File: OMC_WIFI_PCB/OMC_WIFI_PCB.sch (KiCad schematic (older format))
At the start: 19 parts, among them J1 ESP32_Left, J10 Control_ACS712, J11 Control_ZMPT101B, J2 ESP32_Right, J3 Power_In, J4 Switch, J5 Pins_FT232R, J6 Line_Relay, J7 Control_Relay, J8 Line_ACS712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

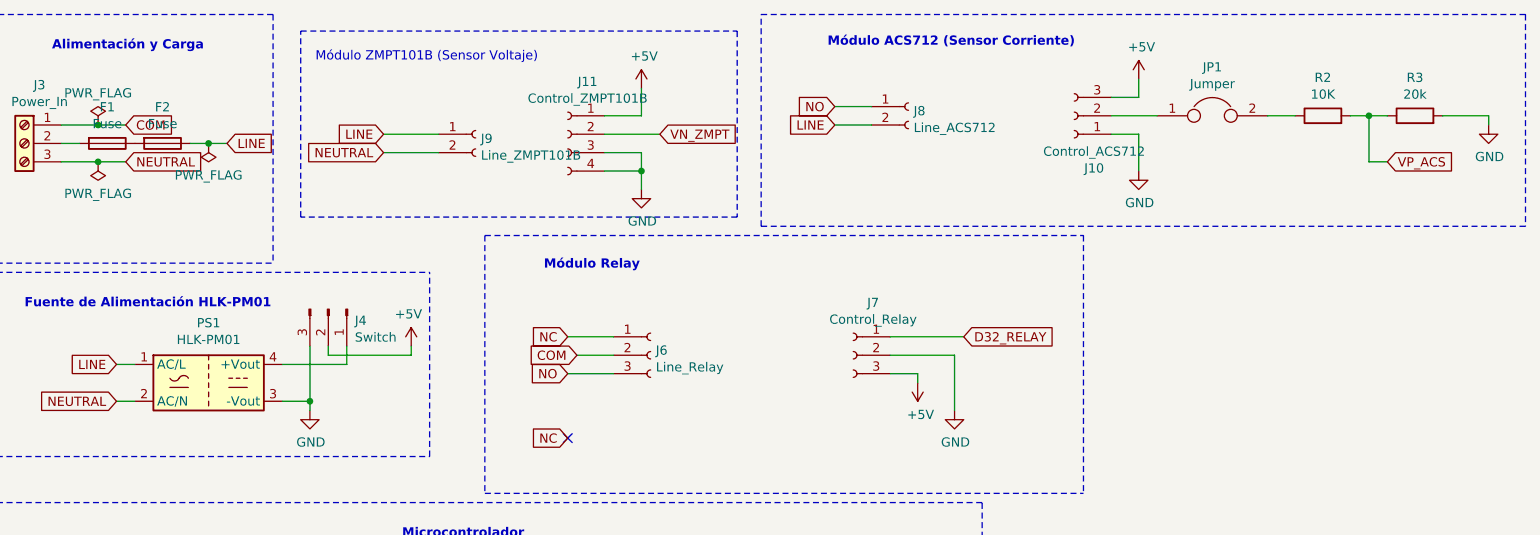
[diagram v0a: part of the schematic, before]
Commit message: Diseño PCB
+ Archivos Gerber y Drill
- Divisor de tensión del ACS712
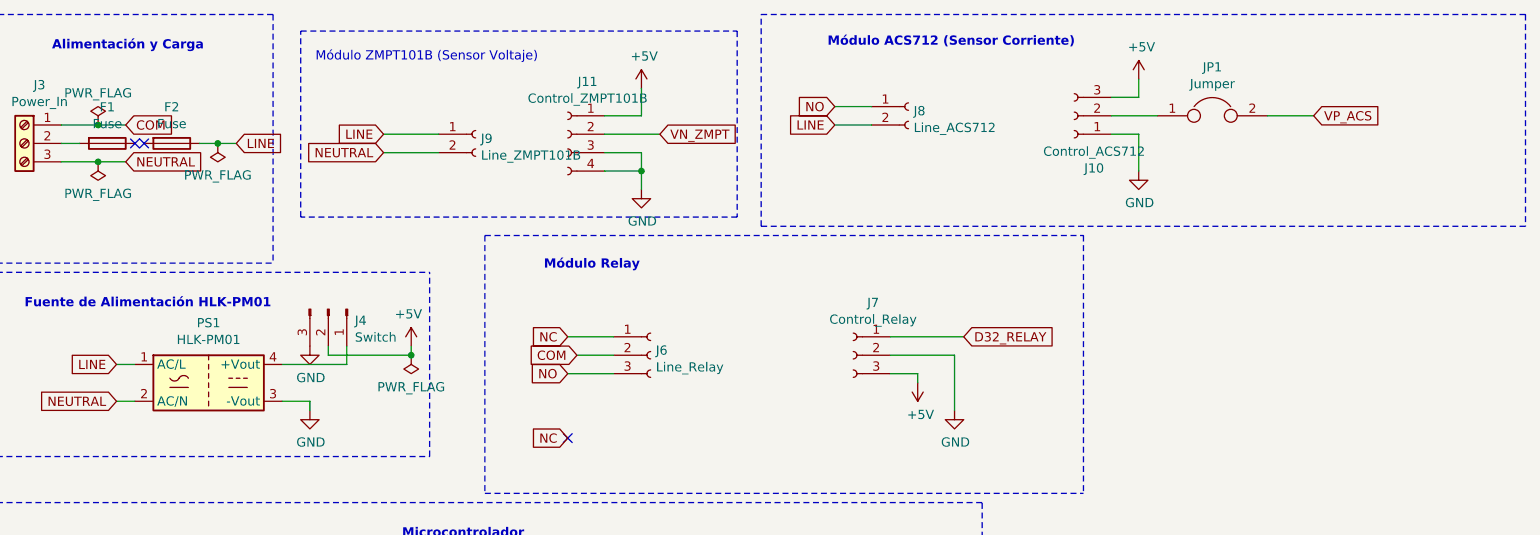
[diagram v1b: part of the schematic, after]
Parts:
- removed R2: 10K, Resistor_SMD:R_2010_5025Metric_Pad1.40x2.65mm_HandSolder, symbol Device:R
- removed R3: 20k, Resistor_SMD:R_2010_5025Metric_Pad1.40x2.65mm_HandSolder, symbol Device:R
- JP1: footprint Connector_PinHeader_1.00mm:PinHeader_1x02_P1.00mm_Vertical -> Connector_PinHeader_2.54mm:PinHeader_1x02_P2.54mm_Vertical
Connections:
- net VP_ACS: now also JP1.2
- net at F1.1: no longer F2.2
- no-connect marks 25 -> 27
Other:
- moved on the sheet: F2
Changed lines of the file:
@@
 	1    0    0    -1
 $EndComp
-Text GLabel 8250 1400 2    50   Input ~ 0
-VP_ACS
 $Comp
 L Connector:Conn_01x03_Female J10
@@
 	700  3000 3050 3000
 Wire Wire Line
-	2400 2400 2400 2700
-Connection ~ 2400 2700
-Wire Wire Line
 	2600 2400 2600 2500
 Wire Wire Line
@@
 L power:PWR_FLAG #FLG0103
 U 1 1 62127B9A
-P 1850 1300
-F 0 "#FLG0103" H 1850 1375 50  0001 C CNN
-F 1 "PWR_FLAG" H 1850 1473 50  0000 C CNN
-F 2 "" H 1850 1300 50  0001 C CNN
-F 3 "~" H 1850 1300 50  0001 C CNN
-	1    1850 1300
+P 1900 1300
+F 0 "#FLG0103" H 1900 1375 50  0001 C CNN
+F 1 "PWR_FLAG" H 1900 1473 50  0000 C CNN
+F 2 "" H 1900 1300 50  0001 C CNN
+F 3 "~" H 1900 1300 50  0001 C CNN
+	1    1900 1300
 	1    0    0    1
 $EndComp
 Wire Wire Line
-	1950 1300 1850 1300
-Wire Wire Line
-	1750 1300 1850 1300
-Connection ~ 1850 1300
+	2000 1300 1900 1300
+Wire Wire Line
+	1800 1300 1900 1300
+Connection ~ 1900 1300
 $Comp
 L Device:Fuse F1
@@
 L Device:Fuse F2
 U 1 1 6214DC3E
-P 1600 1300
-F 0 "F2" V 1403 1300 50  0000 C CNN
-F 1 "Fuse" V 1494 1300 50  0000 C CNN
-F 2 "Fuse:Fuse_Littelfuse_395Series" V 1530 1300 50  0001 C CNN
-F 3 "~" H 1600 1300 50  0001 C CNN
-	1    1600 1300
+P 1650 1300
+F 0 "F2" V 1453 1300 50  0000 C CNN
+F 1 "Fuse" V 1544 1300 50  0000 C CNN
+F 2 "Fuse:Fuse_Littelfuse_395Series" V 1580 1300 50  0001 C CNN
+F 3 "~" H 1650 1300 50  0001 C CNN
+	1    1650 1300
 	0    1    1    0
 $EndComp
-Text GLabel 1950 1300 2    50   Input ~ 0
+Text GLabel 2000 1300 2    50   Input ~ 0
 LINE
 Wire Wire Line
@@
 F 0 "JP1" H 7300 1414 50  0000 C CNN
 F 1 "Jumper" H 7300 1323 50  0000 C CNN
-F 2 "Connector_PinHeader_1.00mm:PinHeader_1x02_P1.00mm_Vertical" H 7300 1150 50  0001 C CNN
+F 2 "Connector_PinHeader_2.54mm:PinHeader_1x02_P2.54mm_Vertical" H 7300 1150 50  0001 C CNN
 F 3 "~" H 7300 1150 50  0001 C CNN
 	1    7300 1150
@@
 Wire Wire Line
 	6750 1150 7000 1150
-$Comp
-L Device:R R2
-U 1 1 621CBE6C
-P 7900 1150
-F 0 "R2" V 8107 1150 50  0000 C CNN
-F 1 "10K" V 8016 1150 50  0000 C CNN
-F 2 "Resistor_SMD:R_2010_5025Metric_Pad1.40x2.65mm_HandSolder" V 7830 1150 50  0001 C CNN
-F 3 "~" H 7900 1150 50  0001 C CNN
-	1    7900 1150
-	0    -1   -1   0
-$EndComp
-$Comp
-L Device:R R3
-U 1 1 621CF98B
-P 8400 1150
-F 0 "R3" V 8607 1150 50  0000 C CNN
-F 1 "20k" V 8516 1150 50  0000 C CNN
-F 2 "Resistor_SMD:R_2010_5025Metric_Pad1.40x2.65mm_HandSolder" V 8330 1150 50  0001 C CNN
-F 3 "~" H 8400 1150 50  0001 C CNN
-	1    8400 1150
-	0    -1   -1   0
-$EndComp
+Wire Notes Line
+	4850 600  9000 600
+Wire Notes Line
+	4850 1750 9000 1750
+Wire Notes Line
+	9000 600  9000 1750
+Text GLabel 7850 1150 2    50   Input ~ 0
+VP_ACS
+Wire Wire Line
+	7600 1150 7850 1150
+$Comp
+L power:PWR_FLAG #FLG0104
+U 1 1 62219A74
+P 2950 2450
+F 0 "#FLG0104" H 2950 2525 50  0001 C CNN
+F 1 "PWR_FLAG" H 2950 2623 50  0000 C CNN
+F 2 "" H 2950 2450 50  0001 C CNN
+F 3 "~" H 2950 2450 50  0001 C CNN
+	1    2950 2450
+	1    0    0    1
+$EndComp
+Connection ~ 2950 2450
 $Comp
 L power:GND #PWR0111
-U 1 1 621D76EE
-P 8800 1200
-F 0 "#PWR0111" H 8800 950 50  0001 C CNN
-F 1 "GND" H 8805 1027 50  0000 C CNN
-F 2 "" H 8800 1200 50  0001 C CNN
-F 3 "" H 8800 1200 50  0001 C CNN
-	1    8800 1200
-	1    0    0    -1
-$EndComp
-Wire Wire Line
-	7600 1150 7750 1150
-Wire Wire Line
-	8050 1150 8150 1150
-Wire Wire Line
-	8550 1150 8800 1150
-Wire Wire Line
-	8800 1150 8800 1200
-Wire Wire Line
-	8250 1400 8150 1400
-Wire Wire Line
-	8150 1400 8150 1150
-Connection ~ 8150 1150
-Wire Wire Line
-	8150 1150 8250 1150
-Wire Notes Line
-	4850 600  9000 600
-Wire Notes Line
-	4850 1750 9000 1750
-Wire Notes Line
-	9000 600  9000 1750
+U 1 1 62227D4B
+P 2400 2400
+F 0 "#PWR0111" H 2400 2150 50  0001 C CNN
+F 1 "GND" H 2405 2227 50  0000 C CNN
+F 2 "" H 2400 2400 50  0001 C CNN
+F 3 "" H 2400 2400 50  0001 C CNN
+	1    2400 2400
+	1    0    0    -1
+$EndComp
+NoConn ~ 1450 1300
+NoConn ~ 1500 1300
 $EndSCHEMATC

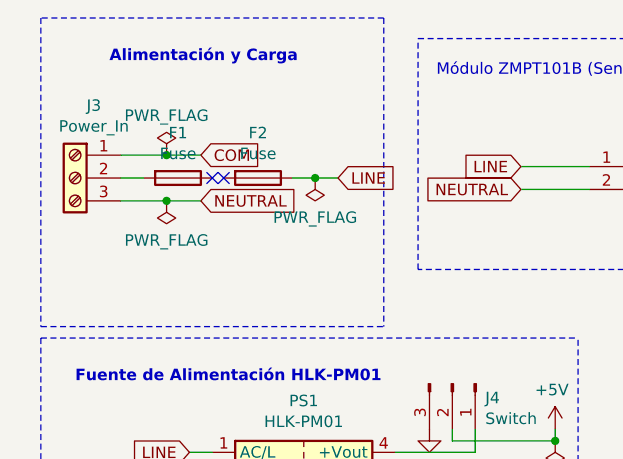
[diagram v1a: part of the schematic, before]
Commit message: Actualización PCB
> Actualización esquemático.
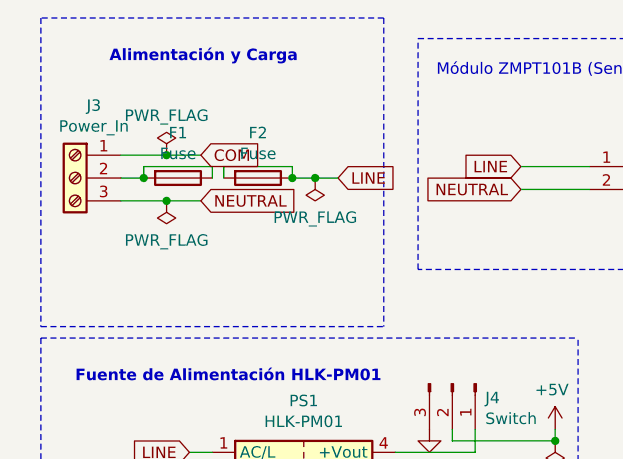
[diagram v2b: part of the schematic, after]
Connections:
- net LINE: now also F2.2
- net at F1.1: now also F1.2, J3.2 (Pin_2)
- no-connect marks 27 -> 25
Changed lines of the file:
@@
 	1    0    0    -1
 $EndComp
-NoConn ~ 1450 1300
-NoConn ~ 1500 1300
+Wire Wire Line
+	1500 1300 1500 1250
+Wire Wire Line
+	1500 1250 1800 1250
+Wire Wire Line
+	1800 1250 1800 1300
+Connection ~ 1800 1300
+Wire Wire Line
+	1450 1300 1450 1250
+Wire Wire Line
+	1450 1250 1150 1250
+Wire Wire Line
+	1150 1250 1150 1300
+Connection ~ 1150 1300
 $EndSCHEMATC

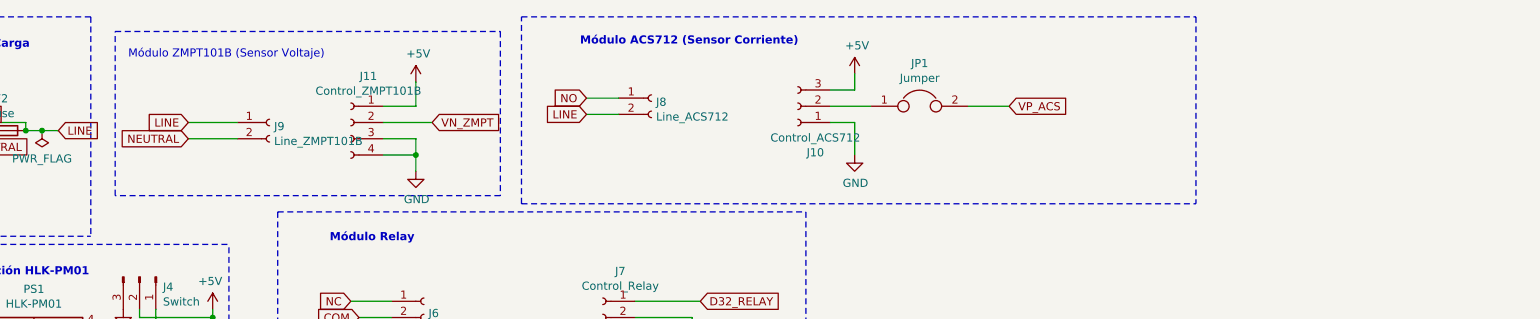
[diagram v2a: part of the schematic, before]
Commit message: Actualización PCB
> Divisores de tensión
> Nuevos Gerbers
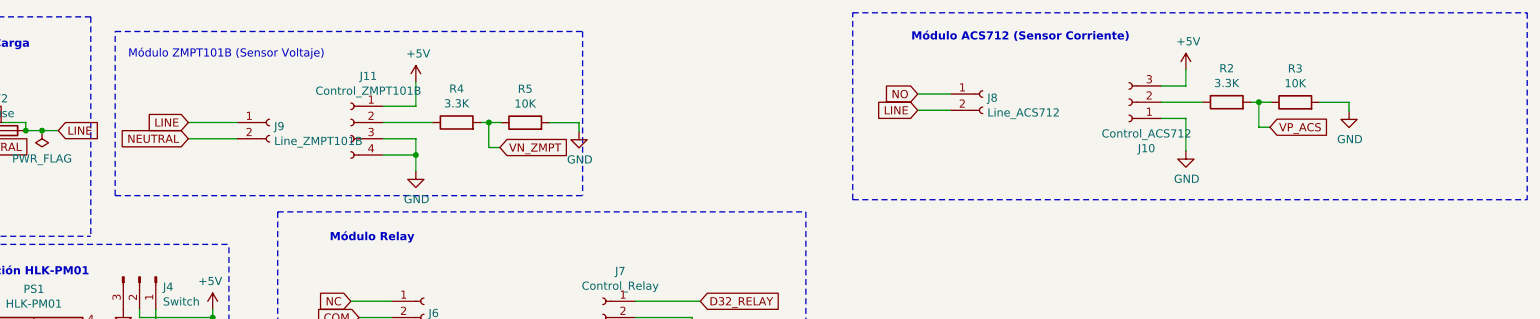
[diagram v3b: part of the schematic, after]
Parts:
- removed JP1: Jumper, Connector_PinHeader_2.54mm:PinHeader_1x02_P2.54mm_Vertical, symbol Device:Jumper
- added R2, R4: 3.3K, Resistor_SMD:R_2010_5025Metric_Pad1.40x2.65mm_HandSolder, symbol Device:R
- added R3, R5: 10K, Resistor_SMD:R_2010_5025Metric_Pad1.40x2.65mm_HandSolder, symbol Device:R
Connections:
- net GND: now also R3.2, R5.2
- net VN_ZMPT: now also R4.2, R5.1; no longer J11.2 (Pin_2)
- net VP_ACS: now also R2.2, R3.1
- net at J10.2 (Pin_2): now also R2.1
- new net: J11.2 (Pin_2), R4.1
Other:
- moved on the sheet: J10, J8
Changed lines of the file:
@@
 	6050 3250 600  3250
 Wire Notes Line
-	4850 1750 4850 600
-Wire Wire Line
-	6900 1050 6900 950
-Wire Wire Line
-	6750 1050 6900 1050
+	6888 1725 6888 575
+Wire Wire Line
+	8938 1025 8938 925
+Wire Wire Line
+	8788 1025 8938 1025
 $Comp
 L power:GND #PWR0110
 U 1 1 620E6BF1
-P 6900 1450
-F 0 "#PWR0110" H 6900 1200 50  0001 C CNN
-F 1 "GND" H 6905 1277 50  0000 C CNN
-F 2 "" H 6900 1450 50  0001 C CNN
-F 3 "" H 6900 1450 50  0001 C CNN
-	1    6900 1450
+P 8938 1425
+F 0 "#PWR0110" H 8938 1175 50  0001 C CNN
+F 1 "GND" H 8943 1252 50  0000 C CNN
+F 2 "" H 8938 1425 50  0001 C CNN
+F 3 "" H 8938 1425 50  0001 C CNN
+	1    8938 1425
 	1    0    0    -1
 $EndComp
@@
 L power:+5V #PWR0109
 U 1 1 620E6405
-P 6900 950
-F 0 "#PWR0109" H 6900 800 50  0001 C CNN
-F 1 "+5V" H 6915 1123 50  0000 C CNN
-F 2 "" H 6900 950 50  0001 C CNN
-F 3 "" H 6900 950 50  0001 C CNN
-	1    6900 950
+P 8938 925
+F 0 "#PWR0109" H 8938 775 50  0001 C CNN
+F 1 "+5V" H 8953 1098 50  0000 C CNN
+F 2 "" H 8938 925 50  0001 C CNN
+F 3 "" H 8938 925 50  0001 C CNN
+	1    8938 925
 	1    0    0    -1
 $EndComp
@@
 L Connector:Conn_01x03_Female J10
 U 1 1 620C97A5
-P 6550 1150
-F 0 "J10" H 6442 1435 50  0000 C CNN
-F 1 "Control_ACS712" H 6442 1344 50  0000 C CNN
-F 2 "Connector_PinHeader_2.54mm:PinHeader_1x03_P2.54mm_Vertical" H 6550 1150 50  0001 C CNN
-F 3 "~" H 6550 1150 50  0001 C CNN
-	1    6550 1150
+P 8588 1125
+F 0 "J10" H 8480 1410 50  0000 C CNN
+F 1 "Control_ACS712" H 8480 1319 50  0000 C CNN
+F 2 "Connector_PinHeader_2.54mm:PinHeader_1x03_P2.54mm_Vertical" H 8588 1125 50  0001 C CNN
+F 3 "~" H 8588 1125 50  0001 C CNN
+	1    8588 1125
 	-1   0    0    1
 $EndComp
-Wire Wire Line
-	4000 1250 4300 1250
-Text GLabel 4300 1250 2    50   Input ~ 0
-VN_ZMPT
 Wire Wire Line
 	4200 1450 4200 1350
@@
 $EndComp
 Wire Notes Line
-	4720 1700 2350 1700
-Wire Notes Line
 	2350 1700 2350 690
 Text Notes 2430 860  0    50   ~ 0
 Módulo ZMPT101B (Sensor Voltaje)\n
-Text Notes 5210 780  0    50   ~ 10
+Text Notes 7248 755  0    50   ~ 10
 Módulo ACS712 (Sensor Corriente)\n
 Wire Notes Line
-	4720 690  4720 1700
-Wire Notes Line
 	6050 7350 6050 3250
 Wire Notes Line
 	600  7350 6050 7350
 Wire Notes Line
-	2350 690  4720 690
-Wire Notes Line
 	700  600  700  1950
 Wire Wire Line
-	5250 1100 5450 1100
+	7288 1075 7488 1075
 Wire Wire Line
 	3100 1350 2800 1350
@@
 Wire Notes Line
 	3350 3200 6600 3200
-Text GLabel 5250 1100 0    50   Input ~ 0
+Text GLabel 7288 1075 0    50   Input ~ 0
 NO
 Text GLabel 1950 6700 0    50   Input ~ 0
@@
 L Connector:Conn_01x02_Female J8
 U 1 1 621188AB
-P 5650 1100
-F 0 "J8" H 5678 1076 50  0000 L CNN
-F 1 "Line_ACS712" H 5678 985 50  0000 L CNN
-F 2 "TerminalBlock:TerminalBlock_bornier-2_P5.08mm" H 5650 1100 50  0001 C CNN
-F 3 "~" H 5650 1100 50  0001 C CNN
-	1    5650 1100
-	1    0    0    -1
-$EndComp
-Wire Wire Line
-	5250 1200 5450 1200
+P 7688 1075
+F 0 "J8" H 7716 1051 50  0000 L CNN
+F 1 "Line_ACS712" H 7716 960 50  0000 L CNN
+F 2 "TerminalBlock:TerminalBlock_bornier-2_P5.08mm" H 7688 1075 50  0001 C CNN
+F 3 "~" H 7688 1075 50  0001 C CNN
+	1    7688 1075
+	1    0    0    -1
+$EndComp
+Wire Wire Line
+	7288 1175 7488 1175
 Wire Notes Line
 	2200 600  2200 1950
@@
 Text GLabel 1350 2500 0    50   Input ~ 0
 LINE
-Text GLabel 5250 1200 0    50   Input ~ 0
+Text GLabel 7288 1175 0    50   Input ~ 0
 LINE
 Text GLabel 2800 1350 0    50   Input ~ 0
@@
 Connection ~ 1250 1400
 Wire Wire Line
-	6750 1250 6900 1250
-Wire Wire Line
-	6900 1250 6900 1450
-$Comp
-L Device:Jumper JP1
-U 1 1 621BDC2F
-P 7300 1150
-F 0 "JP1" H 7300 1414 50  0000 C CNN
-F 1 "Jumper" H 7300 1323 50  0000 C CNN
-F 2 "Connector_PinHeader_2.54mm:PinHeader_1x02_P2.54mm_Vertical" H 7300 1150 50  0001 C CNN
-F 3 "~" H 7300 1150 50  0001 C CNN
-	1    7300 1150
-	1    0    0    -1
-$EndComp
-Wire Wire Line
-	6750 1150 7000 1150
-Wire Notes Line
-	4850 600  9000 600
-Wire Notes Line
-	4850 1750 9000 1750
-Wire Notes Line
-	9000 600  9000 1750
-Text GLabel 7850 1150 2    50   Input ~ 0
-VP_ACS
-Wire Wire Line
-	7600 1150 7850 1150
+	8788 1225 8938 1225
+Wire Wire Line
+	8938 1225 8938 1425
+Wire Notes Line
+	6888 575  11038 575
+Wire Notes Line
+	6888 1725 11038 1725
+Wire Notes Line
+	11038 575  11038 1725
 $Comp
 L power:PWR_FLAG #FLG0104
@@
 	1150 1250 1150 1300
 Connection ~ 1150 1300
+Wire Wire Line
+	8788 1125 9039 1125
+Wire Wire Line
+	9942 1126 9942 1181
+Wire Wire Line
+	9761 1126 9942 1126
+Wire Wire Line
+	9387 1125 9461 1125
+Connection ~ 9387 1125
+Wire Wire Line
+	9387 1279 9387 1125
+Wire Wire Line
+	9455 1279 9387 1279
+Wire Wire Line
+	9339 1125 9387 1125
+Wire Wire Line
+	9461 1125 9461 1126
+$Comp
+L Device:R R3
+U 1 1 62476E7A
+P 9611 1126
+F 0 "R3" V 9818 1126 50  0000 C CNN
+F 1 "10K" V 9727 1126 50  0000 C CNN
+F 2 "Resistor_SMD:R_2010_5025Metric_Pad1.40x2.65mm_HandSolder" V 9541 1126 50  0001 C CNN
+F 3 "~" H 9611 1126 50  0001 C CNN
+	1    9611 1126
+	0    -1   -1   0
+$EndComp
+$Comp
+L power:GND #PWR0112
+U 1 1 624773A1
+P 9942 1181
+F 0 "#PWR0112" H 9942 931 50  0001 C CNN
+F 1 "GND" H 9947 1008 50  0000 C CNN
+F 2 "" H 9942 1181 50  0001 C CNN
+F 3 "" H 9942 1181 50  0001 C CNN
+	1    9942 1181
+	1    0    0    -1
+$EndComp
+$Comp
+L Device:R R2
+U 1 1 6246D72C
+P 9189 1125
+F 0 "R2" V 9396 1125 50  0000 C CNN
+F 1 "3.3K" V 9305 1125 50  0000 C CNN
+F 2 "Resistor_SMD:R_2010_5025Metric_Pad1.40x2.65mm_HandSolder" V 9119 1125 50  0001 C CNN
+F 3 "~" H 9189 1125 50  0001 C CNN
+	1    9189 1125
+	0    -1   -1   0
+$EndComp
+Text GLabel 9455 1279 2    50   Input ~ 0
+VP_ACS
+Wire Wire Line
+	5204 1251 5204 1306
+Wire Wire Line
+	5023 1251 5204 1251
+Wire Wire Line
+	4649 1250 4723 1250
+Connection ~ 4649 1250
+Wire Wire Line
+	4649 1404 4649 1250
+Wire Wire Line
+	4717 1404 4649 1404
+Wire Wire Line
+	4601 1250 4649 1250
+Wire Wire Line
+	4723 1250 4723 1251
+$Comp
+L Device:R R5
+U 1 1 624E965B
+P 4873 1251
+F 0 "R5" V 5080 1251 50  0000 C CNN
+F 1 "10K" V 4989 1251 50  0000 C CNN
+F 2 "Resistor_SMD:R_2010_5025Metric_Pad1.40x2.65mm_HandSolder" V 4803 1251 50  0001 C CNN
+F 3 "~" H 4873 1251 50  0001 C CNN
+	1    4873 1251
+	0    -1   -1   0
+$EndComp
+$Comp
+L power:GND #PWR0113
+U 1 1 624E9661
+P 5204 1306
+F 0 "#PWR0113" H 5204 1056 50  0001 C CNN
+F 1 "GND" H 5209 1133 50  0000 C CNN
+F 2 "" H 5204 1306 50  0001 C CNN
+F 3 "" H 5204 1306 50  0001 C CNN
+	1    5204 1306
+	1    0    0    -1
+$EndComp
+$Comp
+L Device:R R4
+U 1 1 624E9667
+P 4451 1250
+F 0 "R4" V 4658 1250 50  0000 C CNN
+F 1 "3.3K" V 4567 1250 50  0000 C CNN
+F 2 "Resistor_SMD:R_2010_5025Metric_Pad1.40x2.65mm_HandSolder" V 4381 1250 50  0001 C CNN
+F 3 "~" H 4451 1250 50  0001 C CNN
+	1    4451 1250
+	0    -1   -1   0
+$EndComp
+Text GLabel 4717 1404 2    50   Input ~ 0
+VN_ZMPT
+Wire Wire Line
+	4000 1250 4301 1250
+Wire Notes Line
+	5226 690  5226 1700
+Wire Notes Line
+	2350 1700 5226 1700
+Wire Notes Line
+	2350 690  5226 690
 $EndSCHEMATC
